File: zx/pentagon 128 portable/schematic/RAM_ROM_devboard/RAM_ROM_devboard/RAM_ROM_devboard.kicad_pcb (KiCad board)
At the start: 2 copper layers, 8 parts, among them IC1 IS62C1024AL-35QLI, IC2 SN74AHCT04D, J1 Conn_02x14_Odd_Even, J2 8432-11B1-RK-TP, J3 Conn_02x08_Odd_Even, J4 Conn_02x04_Odd_Even, J5 Conn_02x06_Odd_Even, J6 Conn_02x06_Odd_Even

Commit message: updated board and notes
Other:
- board outline added: 50.5 x 57.9 mm

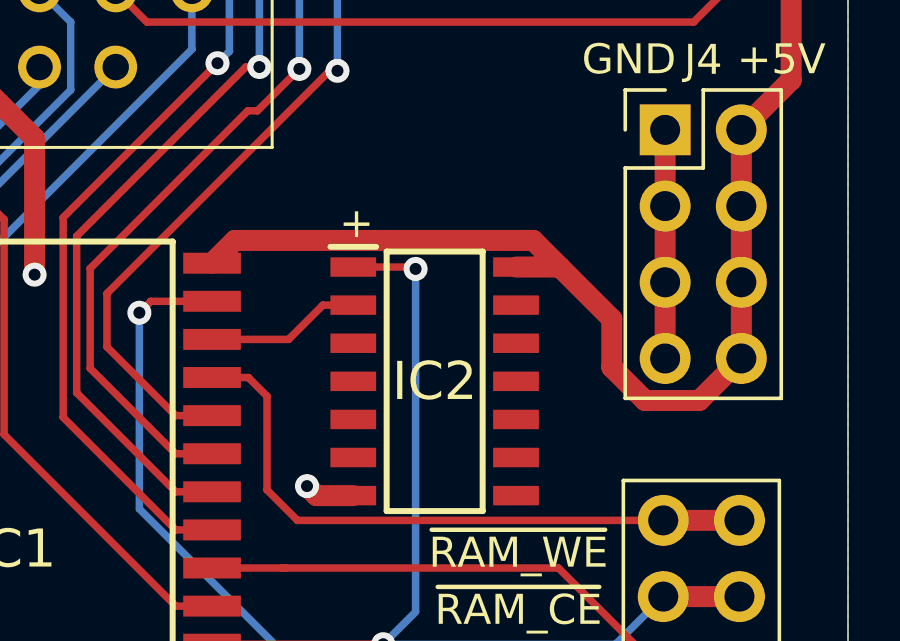
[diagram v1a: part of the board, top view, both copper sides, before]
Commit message: added ZX Keyboard
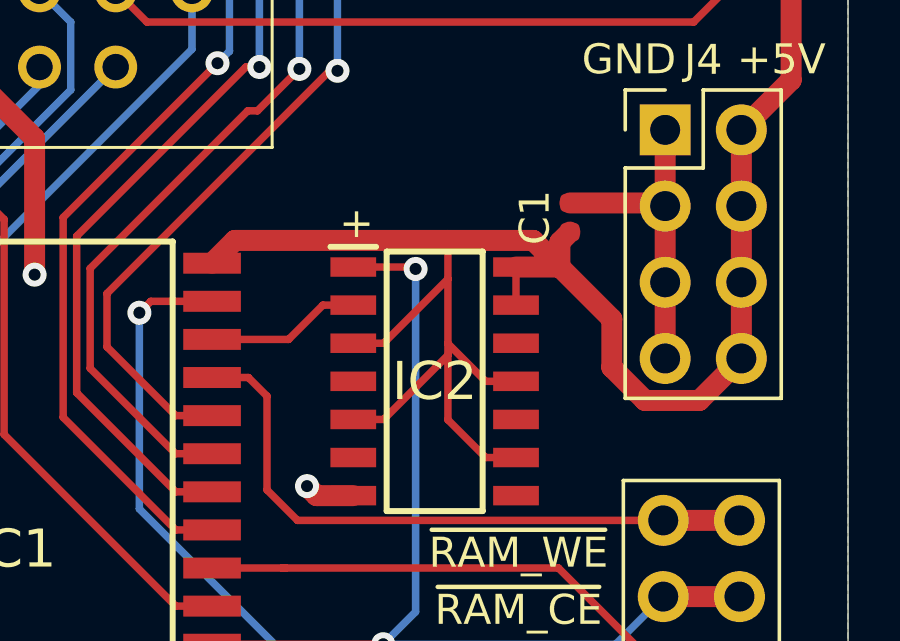
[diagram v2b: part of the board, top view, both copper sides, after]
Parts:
- added C1: C_Small, Capacitor_SMD:C_0402_1005Metric, F.Cu at (137.7, 89.5)
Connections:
- IC2 pad 11: (no net) -> +5V
- IC2 pad 13: (no net) -> +5V
- IC2 pad 3: (no net) -> +5V
- IC2 pad 5: (no net) -> +5V
- IC2 pad 9: (no net) -> +5V
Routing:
- net +5V: track 78.8 -> 101.1 mm
- net GND: track 19.0 -> 22.2 mm
